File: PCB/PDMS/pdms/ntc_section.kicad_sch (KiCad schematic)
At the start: 11 parts, among them IC18 NX3L4051PW,118

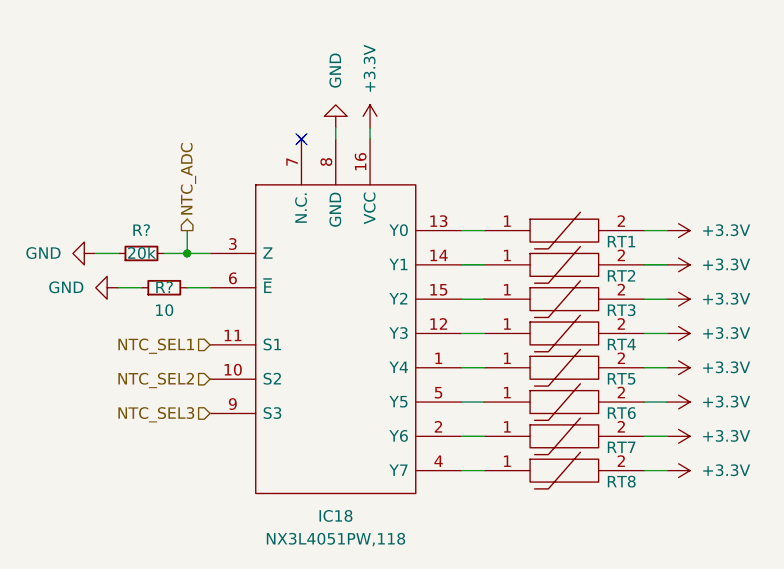
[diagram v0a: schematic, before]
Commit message: Changed MCU to L496 & finished powerswitch section
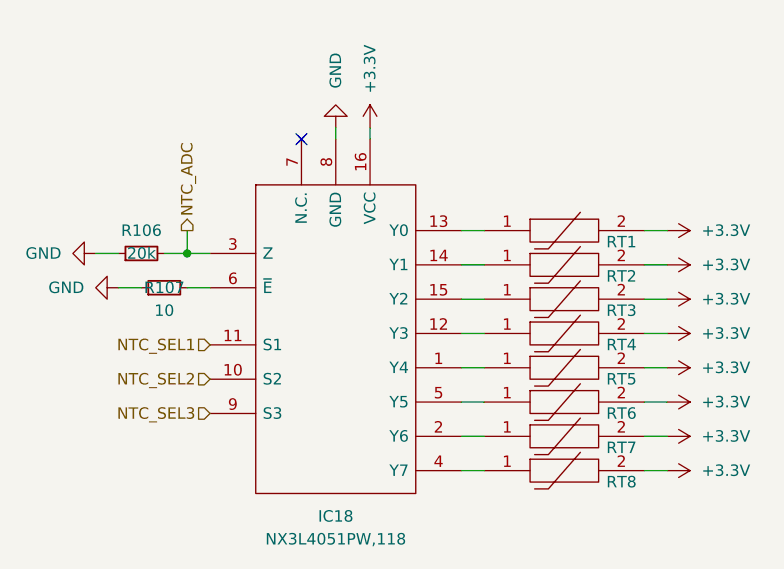
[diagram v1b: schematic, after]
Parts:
- gave numbers to parts that had none: 2
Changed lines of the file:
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@@
   (symbol (lib_id "Device:R_Small") (at 54.61 57.15 90) (unit 1)
     (in_bom yes) (on_board yes)
-    (property "Reference" "R?" (id 0) (at 54.61 54.61 90))
+    (property "Reference" "R106" (id 0) (at 54.61 54.61 90))
     (property "Value" "20k" (id 1) (at 54.61 57.15 90))
     (property "Footprint" "" (id 2) (at 54.61 57.15 0)
@@
   (symbol (lib_id "power:GND") (at 52.07 60.96 270) (unit 1)
     (in_bom yes) (on_board yes) (fields_autoplaced)
-    (property "Reference" "#PWR?" (id 0) (at 45.72 60.96 0)
+    (property "Reference" "#PWR0309" (id 0) (at 45.72 60.96 0)
       (effects (font (size 1.27 1.27)) hide)
     )
@@
   (symbol (lib_id "power:GND") (at 49.53 57.15 270) (unit 1)
     (in_bom yes) (on_board yes) (fields_autoplaced)
-    (property "Reference" "#PWR?" (id 0) (at 43.18 57.15 0)
+    (property "Reference" "#PWR0310" (id 0) (at 43.18 57.15 0)
       (effects (font (size 1.27 1.27)) hide)
     )
@@
   (symbol (lib_id "power:GND") (at 76.2 43.18 180) (unit 1)
     (in_bom yes) (on_board yes)
-    (property "Reference" "#PWR?" (id 0) (at 76.2 36.83 0)
+    (property "Reference" "#PWR0312" (id 0) (at 76.2 36.83 0)
       (effects (font (size 1.27 1.27)) hide)
     )
@@
   (symbol (lib_id "power:+3.3V") (at 80.01 43.18 0) (unit 1)
     (in_bom yes) (on_board yes)
-    (property "Reference" "#PWR?" (id 0) (at 80.01 46.99 0)
+    (property "Reference" "#PWR0311" (id 0) (at 80.01 46.99 0)
       (effects (font (size 1.27 1.27)) hide)
     )
@@
   (symbol (lib_id "Device:R_Small") (at 57.15 60.96 90) (unit 1)
     (in_bom yes) (on_board yes)
-    (property "Reference" "R?" (id 0) (at 57.15 60.96 90))
+    (property "Reference" "R107" (id 0) (at 57.15 60.96 90))
     (property "Value" "10" (id 1) (at 57.15 63.5 90))
     (property "Footprint" "" (id 2) (at 57.15 60.96 0)

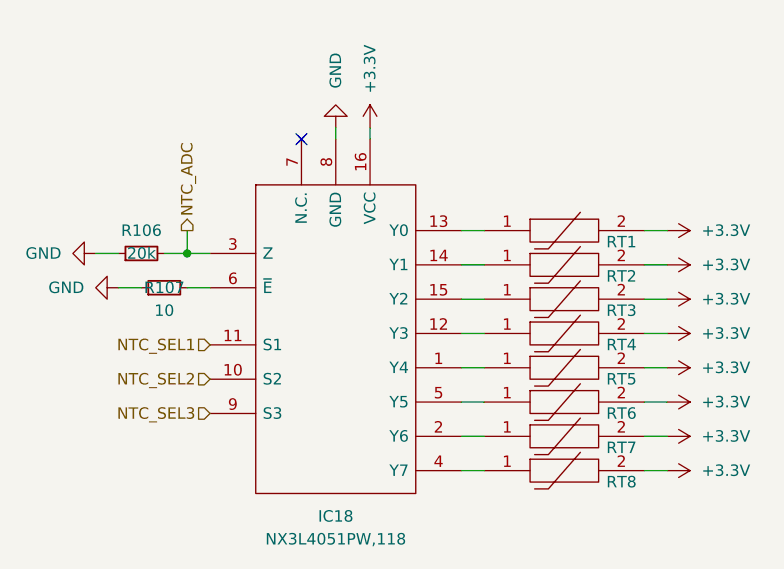
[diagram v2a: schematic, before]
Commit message: Wired all peripherals
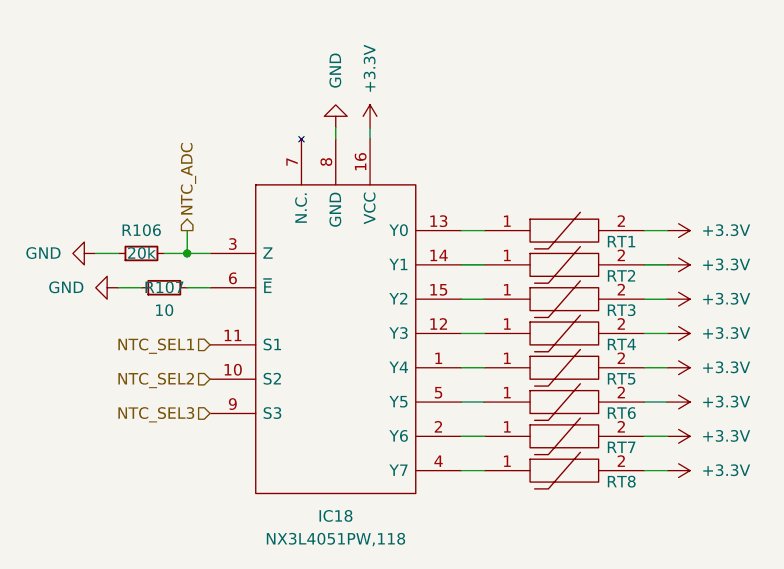
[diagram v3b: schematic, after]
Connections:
- no-connect marks 1 -> 0
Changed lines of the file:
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@@
   (junction (at 59.69 57.15) (diameter 0) (color 0 0 0 0)
   )
-  (no_connect (at 72.39 44.45))
   (wire (pts (xy 59.69 60.96) (xy 62.23 60.96))
     (stroke (width 0) (type default) (color 0 0 0 0))
@@
     (stroke (width 0) (type default) (color 0 0 0 0))
   )
+  (hierarchical_label "NTC_ADC" (shape output) (at 59.69 54.61 90)
+    (effects (font (size 1.27 1.27)) (justify left))
+  )
+  (hierarchical_label "NTC_SEL3" (shape input) (at 62.23 74.93 180)
+    (effects (font (size 1.27 1.27)) (justify right))
+  )
   (hierarchical_label "NTC_SEL1" (shape input) (at 62.23 67.31 180)
     (effects (font (size 1.27 1.27)) (justify right))
-  )
-  (hierarchical_label "NTC_ADC" (shape output) (at 59.69 54.61 90)
-    (effects (font (size 1.27 1.27)) (justify left))
   )
   (hierarchical_label "NTC_SEL2" (shape input) (at 62.23 71.12 180)
     (effects (font (size 1.27 1.27)) (justify right))
   )
-  (hierarchical_label "NTC_SEL3" (shape input) (at 62.23 74.93 180)
-    (effects (font (size 1.27 1.27)) (justify right))
-  )

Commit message: Mostly assigned footprints
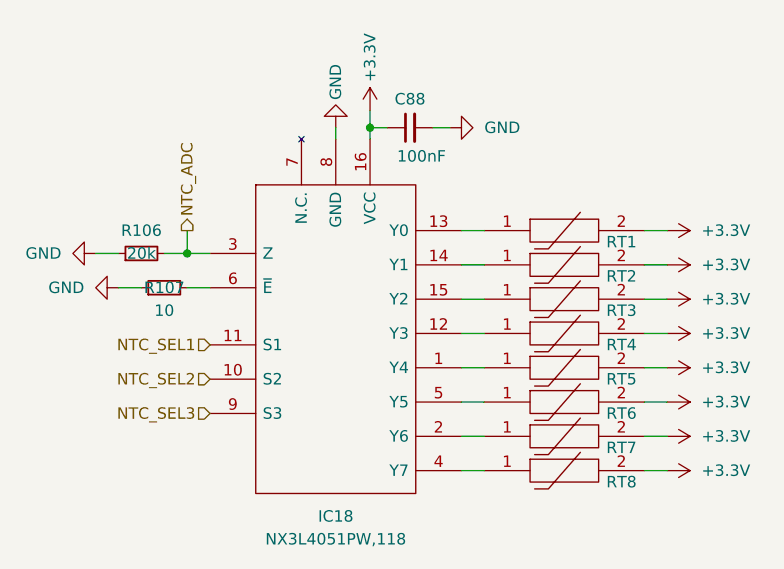
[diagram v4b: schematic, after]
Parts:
- added C88: 100nF, Capacitor_SMD:C_0402_1005Metric_Pad0.74x0.62mm_HandSolder, symbol Device:C_Small
- IC18: footprint (none) -> PDMS_Additional:SOP65P640X110-16N
- RT1, RT2, RT3, RT4, RT5, RT6, RT7, RT8: footprint (none) -> PDMS_Additional:THRMC1005X60N
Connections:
- net +3.3V: now also C88.1
- net GND: now also C88.2

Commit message: Crucial fully assigned schematics
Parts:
- R106, R107: footprint (none) -> Resistor_SMD:R_0402_1005Metric
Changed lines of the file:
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@@
     (property "Reference" "R106" (id 0) (at 54.61 54.61 90))
     (property "Value" "20k" (id 1) (at 54.61 57.15 90))
-    (property "Footprint" "" (id 2) (at 54.61 57.15 0)
+    (property "Footprint" "Resistor_SMD:R_0402_1005Metric" (id 2) (at 54.61 57.15 0)
       (effects (font (size 1.27 1.27)) hide)
     )
@@
     (property "Reference" "R107" (id 0) (at 57.15 60.96 90))
     (property "Value" "10" (id 1) (at 57.15 63.5 90))
-    (property "Footprint" "" (id 2) (at 57.15 60.96 0)
-      (effects (font (size 1.27 1.27)) hide)
-    )
+    (property "Footprint" "Resistor_SMD:R_0402_1005Metric" (id 2) (at 57.15 60.96 0)
+      (effects (font (size 1.27 1.27)) hide)
+    )
